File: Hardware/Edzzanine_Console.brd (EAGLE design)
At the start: 30.5 x 44.5 mm, 32 parts, among them U1 MIC5219 3.3V, U2 FTS31XS-U

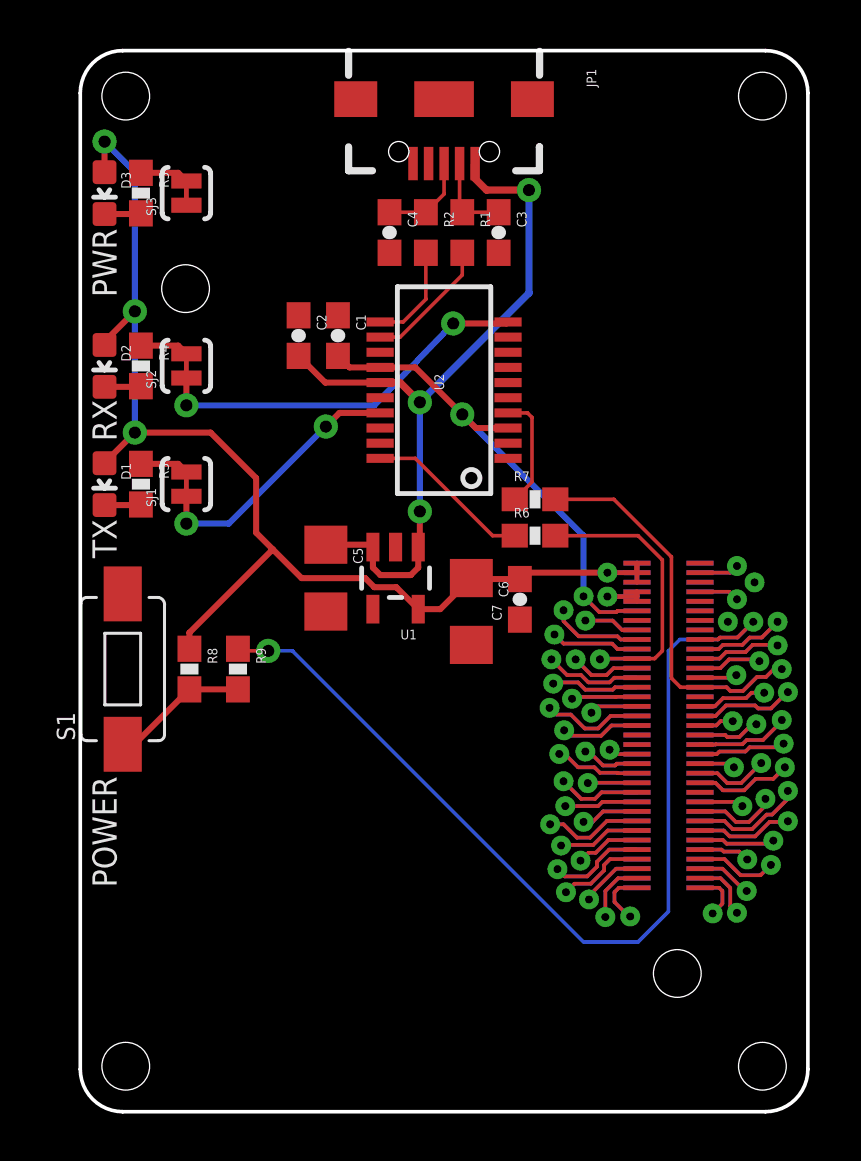
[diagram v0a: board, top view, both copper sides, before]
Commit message: replaced power supply with something more powerful. added fiducials
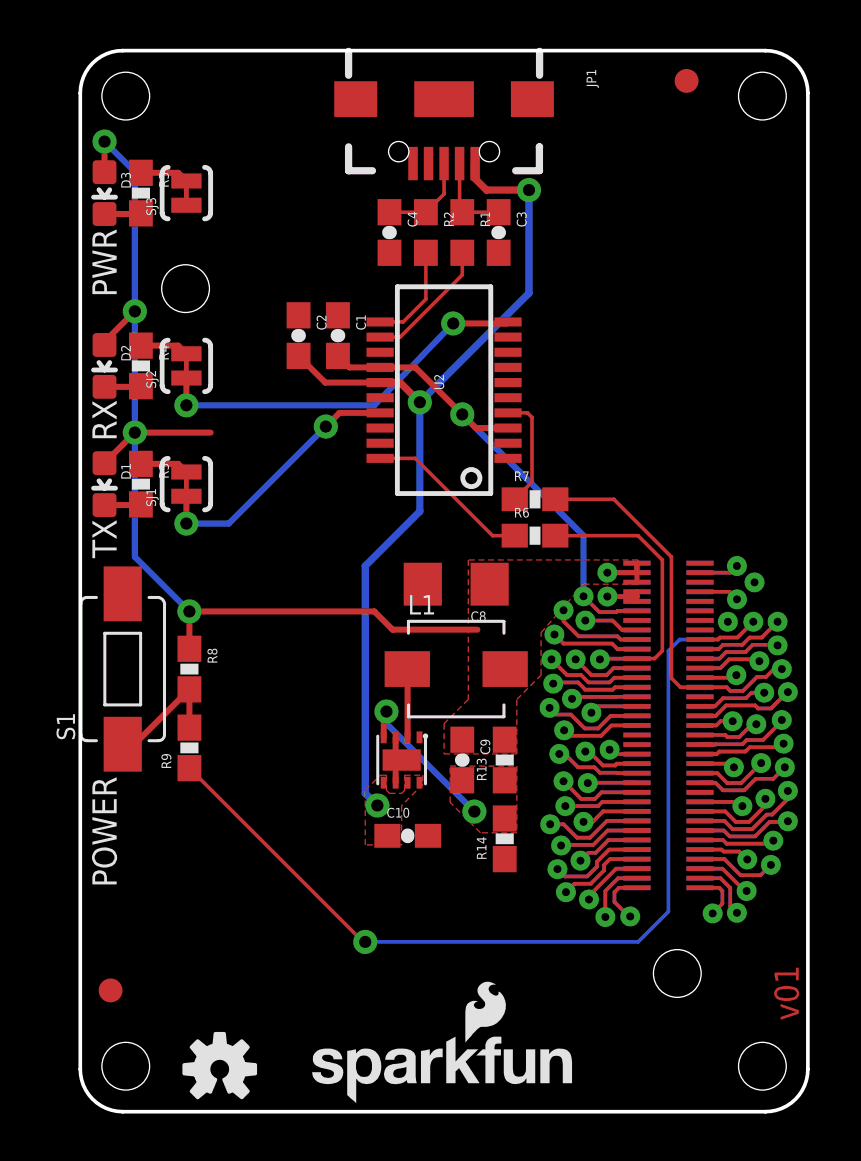
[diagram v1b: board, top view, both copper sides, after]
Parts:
- removed C5, C6: 10uF, SparkFun-Capacitors:1206
- removed C7: 0.1uF, SparkFun-Capacitors:0603-CAP
- removed U1: MIC5219 3.3V, SparkFun-PowerIC:SOT23-5
- added C10: 4.7uF, SparkFun-Capacitors:0603-CAP
- added C8: 10uF, SparkFun-Capacitors:1206
- added C9: 9.0pF, SparkFun-Capacitors:0603-CAP
- added FID1, FID2: FIDUCIAL1X2, SparkFun-Aesthetics:FIDUCIAL-1X2
- added L1: (no value), SparkFun-Passives:INDUCTOR-SRP4020
- added LOGO1: SFE_LOGO_NAME_FLAME.1_INCH, SparkFun-Aesthetics:SFE_LOGO_NAME_FLAME_.1
- added LOGO4: OSHW-LOGOS, SparkFun-Aesthetics:OSHW-LOGO-S
- added R13: 680k, SparkFun-Resistors:0603-RES
- added R14: 120k, SparkFun-Resistors:0603-RES
- added U4: TPS62065, Testing:WSON-8-PAD
- moved R9 3.88 mm to (4.57, 15.2), turned to 90 degrees
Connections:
- new net N$18: C9.2, R13.1, R14.2, U4.4
- new net N$19: L1.P$1, U4.2
- net 5V: now also C10.1, U4.5, U4.7, U4.8; no longer C5.1, U1.1, U1.3
- net GND: now also C10.2, C8.2, R14.1, U4.1, U4.3, U4.6, U4.PAD; no longer C5.2, C6.2, C7.1, U1.2
- net VSYS: now also C8.1, C9.1, L1.P$2, R13.2; no longer C6.1, C7.2, U1.5
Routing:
- net N$18: track 0.00 -> 6.85 mm, vias 0 -> 2
- net 5V: track 31.8 -> 37.8 mm
- net VSYS: track 52.7 -> 47.8 mm, vias 4 -> 5
- net N$19: track 0.00 -> 2.87 mm
- net GND: track 0.00 -> 2.11 mm
- added copper zone on layer 1, net 5V
- added copper zone on layer 1, net N$18
- added copper zone on layer 1, net VSYS
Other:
- board text added: "Edzzanine Console"
- board text added: "v01"
- board text removed: "Edizzine Console"

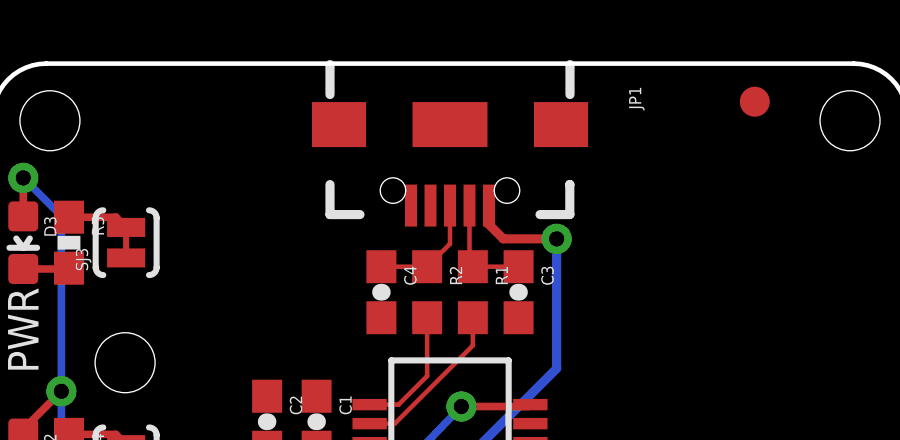
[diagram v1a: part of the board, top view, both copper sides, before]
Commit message: added vias to usb connectors for better staking.
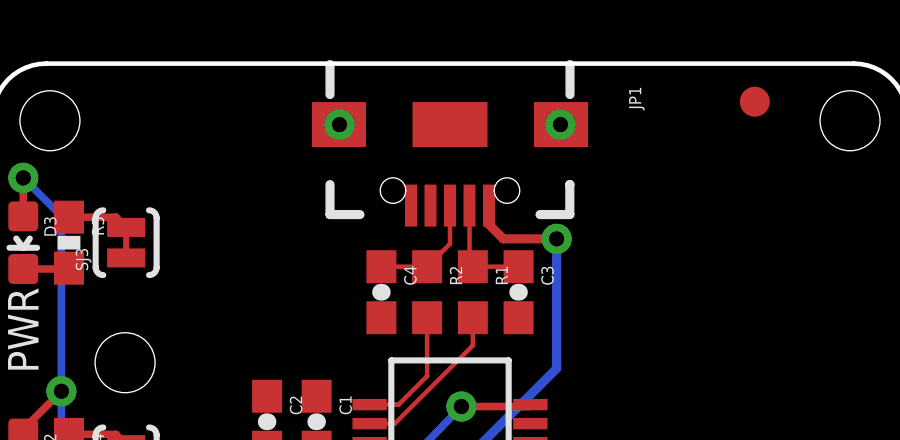
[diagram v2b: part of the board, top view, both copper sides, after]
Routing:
- net GND: vias 2 -> 4
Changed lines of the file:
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@@
 <setting verticaltext="up"/>
 </settings>
-<grid distance="0.05" unitdist="inch" unit="inch" style="lines" multiple="1" display="yes" altdistance="0.005" altunitdist="inch" altunit="inch"/>
+<grid distance="0.005" unitdist="inch" unit="inch" style="lines" multiple="1" display="yes" altdistance="0.005" altunitdist="inch" altunit="inch"/>
 <layers>
 <layer number="1" name="Top" color="4" fill="1" visible="yes" active="yes"/>
@@
 <wire x1="13.212" y1="13.782" x2="13.212" y2="14.482" width="0.254" layer="1"/>
 <wire x1="13.212" y1="14.482" x2="13.462" y2="14.732" width="0.254" layer="1"/>
+<via x="11.557" y="42.418" extent="1-16" drill="0.508"/>
+<via x="18.923" y="42.418" extent="1-16" drill="0.508"/>
+<wire x1="18.94" y1="42.418" x2="18.923" y2="42.418" width="0" layer="19" extent="1-1"/>
 </signal>
 <signal name="VSYS">

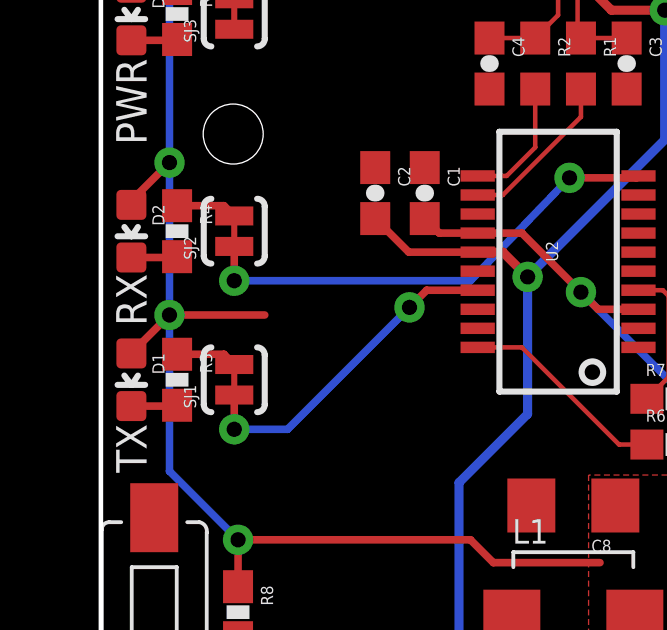
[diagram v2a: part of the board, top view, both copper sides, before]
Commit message: removed stray trace
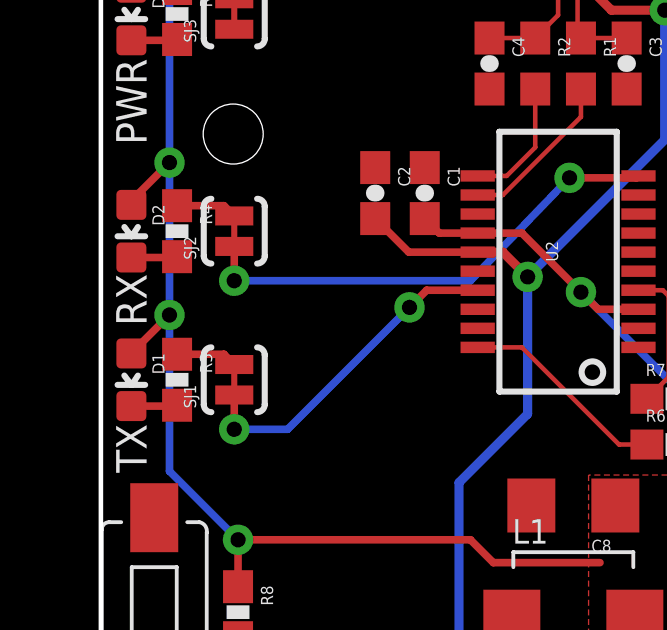
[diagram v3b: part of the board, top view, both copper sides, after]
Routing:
- net VSYS: track 47.8 -> 44.6 mm
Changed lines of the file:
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@@
 <via x="11.557" y="42.418" extent="1-16" drill="0.508"/>
 <via x="18.923" y="42.418" extent="1-16" drill="0.508"/>
-<wire x1="18.94" y1="42.418" x2="18.923" y2="42.418" width="0" layer="19" extent="1-1"/>
 </signal>
 <signal name="VSYS">
@@
 <wire x1="1.016" y1="40.64" x2="2.286" y2="39.37" width="0.254" layer="16"/>
 <wire x1="2.286" y1="39.37" x2="2.286" y2="33.528" width="0.254" layer="16"/>
-<wire x1="2.286" y1="28.448" x2="5.461" y2="28.448" width="0.254" layer="1"/>
 <contactref element="R8" pad="1"/>
 <wire x1="4.572" y1="19.392" x2="4.572" y2="20.955" width="0.254" layer="1"/>
